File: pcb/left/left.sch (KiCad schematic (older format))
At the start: 96 parts

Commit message: pcb: left: schema
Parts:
- added D?: LED_Small, symbol Device:LED_Small
- added R?: 10K, symbol Device:R_Small
- added R?: 470, symbol Device:R_Small
- added U?: MCP23018_SO, Package_SO:SOIC-28W_7.5x17.9mm_P1.27mm, symbol symbols:MCP23018_SO
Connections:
- net labels added: COL0, COL1, COL10, COL2, COL3, COL4, COL5, COL6, COL7, COL8, COL9, ROW0, ROW1, ROW2, ROW3
- wire segments 144 -> 149
- no-connect marks 0 -> 2
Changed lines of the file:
@@
 	6650 1300 6150 1300
 Connection ~ 6650 1300
+$Comp
+L symbols:MCP23018_SO U?
+U 1 1 603DE333
+P 2350 4150
+F 0 "U?" H 2300 3800 50  0000 C CNN
+F 1 "MCP23018_SO" H 2200 3650 50  0000 C CNN
+F 2 "Package_SO:SOIC-28W_7.5x17.9mm_P1.27mm" H 2550 3150 50  0001 L CNN
+F 3 "http://ww1.microchip.com/downloads/en/DeviceDoc/20001952C.pdf" H 2550 3050 50  0001 L CNN
+	1    2350 4150
+	1    0    0    -1
+$EndComp
+$Comp
+L power:GND #PWR?
+U 1 1 603E8C90
+P 2350 5250
+F 0 "#PWR?" H 2350 5000 50  0001 C CNN
+F 1 "GND" H 2355 5077 50  0000 C CNN
+F 2 "" H 2350 5250 50  0001 C CNN
+F 3 "" H 2350 5250 50  0001 C CNN
+	1    2350 5250
+	1    0    0    -1
+$EndComp
+$Comp
+L power:GND #PWR?
+U 1 1 603F7DD2
+P 1650 4950
+F 0 "#PWR?" H 1650 4700 50  0001 C CNN
+F 1 "GND" H 1655 4777 50  0000 C CNN
+F 2 "" H 1650 4950 50  0001 C CNN
+F 3 "" H 1650 4950 50  0001 C CNN
+	1    1650 4950
+	1    0    0    -1
+$EndComp
+NoConn ~ 1650 3850
+NoConn ~ 1650 3950
+$Comp
+L power:+5V #PWR?
+U 1 1 6040C295
+P 1150 4300
+F 0 "#PWR?" H 1150 4150 50  0001 C CNN
+F 1 "+5V" H 1165 4473 50  0000 C CNN
+F 2 "" H 1150 4300 50  0001 C CNN
+F 3 "" H 1150 4300 50  0001 C CNN
+	1    1150 4300
+	1    0    0    -1
+$EndComp
+$Comp
+L Device:R_Small R?
+U 1 1 6040E182
+P 1400 4300
+F 0 "R?" V 1204 4300 50  0000 C CNN
+F 1 "10K" V 1295 4300 50  0000 C CNN
+F 2 "" H 1400 4300 50  0001 C CNN
+F 3 "~" H 1400 4300 50  0001 C CNN
+	1    1400 4300
+	0    1    1    0
+$EndComp
+Wire Wire Line
+	1150 4300 1300 4300
+Wire Wire Line
+	1500 4300 1650 4300
+$Comp
+L power:+5V #PWR?
+U 1 1 60422DB8
+P 2350 3050
+F 0 "#PWR?" H 2350 2900 50  0001 C CNN
+F 1 "+5V" H 2365 3223 50  0000 C CNN
+F 2 "" H 2350 3050 50  0001 C CNN
+F 3 "" H 2350 3050 50  0001 C CNN
+	1    2350 3050
+	1    0    0    -1
+$EndComp
+Text Label 1450 3350 0    50   ~ 0
+SCL
+Text Label 1450 3450 0    50   ~ 0
+SDA
+Wire Wire Line
+	1450 3350 1650 3350
+Wire Wire Line
+	1450 3450 1650 3450
+Text Label 6150 1300 0    50   ~ 0
+COL0
+Text Label 6150 1950 0    50   ~ 0
+COL1
+Text Label 6150 2600 0    50   ~ 0
+COL2
+Text Label 6150 3250 0    50   ~ 0
+COL3
+Text Label 6150 3900 0    50   ~ 0
+COL4
+Text Label 10600 4550 2    50   ~ 0
+COL5
+Text Label 10600 3900 2    50   ~ 0
+COL6
+Text Label 10600 3250 2    50   ~ 0
+COL7
+Text Label 10600 2600 2    50   ~ 0
+COL8
+Text Label 10600 1950 2    50   ~ 0
+COL9
+Text Label 10600 1300 2    50   ~ 0
+COL10
+Text Label 6850 4800 1    50   ~ 0
+ROW0
+Text Label 7250 4800 1    50   ~ 0
+ROW1
+Text Label 7650 4800 1    50   ~ 0
+ROW2
+Text Label 8050 4800 1    50   ~ 0
+ROW3
+Text Label 3050 4250 0    50   ~ 0
+COL0
+Text Label 3050 4350 0    50   ~ 0
+COL1
+Text Label 3050 4450 0    50   ~ 0
+COL2
+Text Label 3050 4550 0    50   ~ 0
+COL3
+Text Label 3050 4650 0    50   ~ 0
+COL4
+Text Label 3050 4750 0    50   ~ 0
+COL5
+Text Label 3050 4850 0    50   ~ 0
+COL6
+Text Label 3050 4950 0    50   ~ 0
+COL7
+Text Label 3050 3350 0    50   ~ 0
+COL8
+Text Label 3050 3450 0    50   ~ 0
+COL9
+Text Label 3050 3550 0    50   ~ 0
+COL10
+Text Label 3050 3650 0    50   ~ 0
+ROW0
+Text Label 3050 3750 0    50   ~ 0
+ROW1
+Text Label 3050 3850 0    50   ~ 0
+ROW2
+Text Label 3050 3950 0    50   ~ 0
+ROW3
+Wire Wire Line
+	3050 4050 3600 4050
+$Comp
+L Device:LED_Small D?
+U 1 1 604A9BDF
+P 3600 3950
+F 0 "D?" V 3646 3880 50  0000 R CNN
+F 1 "LED_Small" V 3555 3880 50  0000 R CNN
+F 2 "" V 3600 3950 50  0001 C CNN
+F 3 "~" V 3600 3950 50  0001 C CNN
+	1    3600 3950
+	0    -1   -1   0
+$EndComp
+$Comp
+L Device:R_Small R?
+U 1 1 604AA823
+P 3600 3750
+F 0 "R?" H 3659 3796 50  0000 L CNN
+F 1 "470" H 3659 3705 50  0000 L CNN
+F 2 "" H 3600 3750 50  0001 C CNN
+F 3 "~" H 3600 3750 50  0001 C CNN
+	1    3600 3750
+	1    0    0    -1
+$EndComp
+$Comp
+L power:+5V #PWR?
+U 1 1 604AB14C
+P 3600 3650
+F 0 "#PWR?" H 3600 3500 50  0001 C CNN
+F 1 "+5V" H 3615 3823 50  0000 C CNN
+F 2 "" H 3600 3650 50  0001 C CNN
+F 3 "" H 3600 3650 50  0001 C CNN
+	1    3600 3650
+	1    0    0    -1
+$EndComp
 $EndSCHEMATC

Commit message: pcb: left: annotate
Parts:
- gave numbers to parts that had none: 100
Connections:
- no-connect marks 2 -> 3

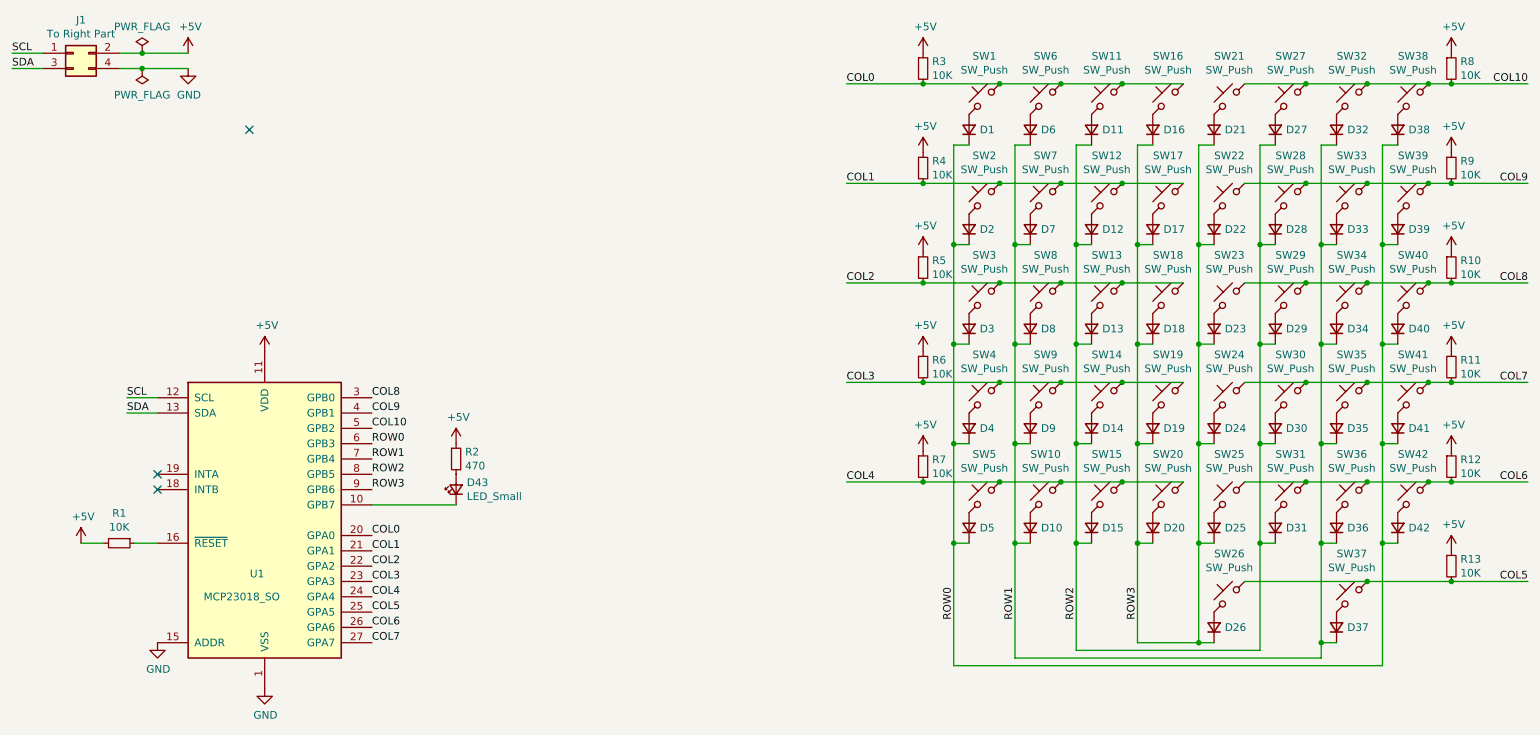
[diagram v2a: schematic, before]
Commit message: pcb: left: assign footprints
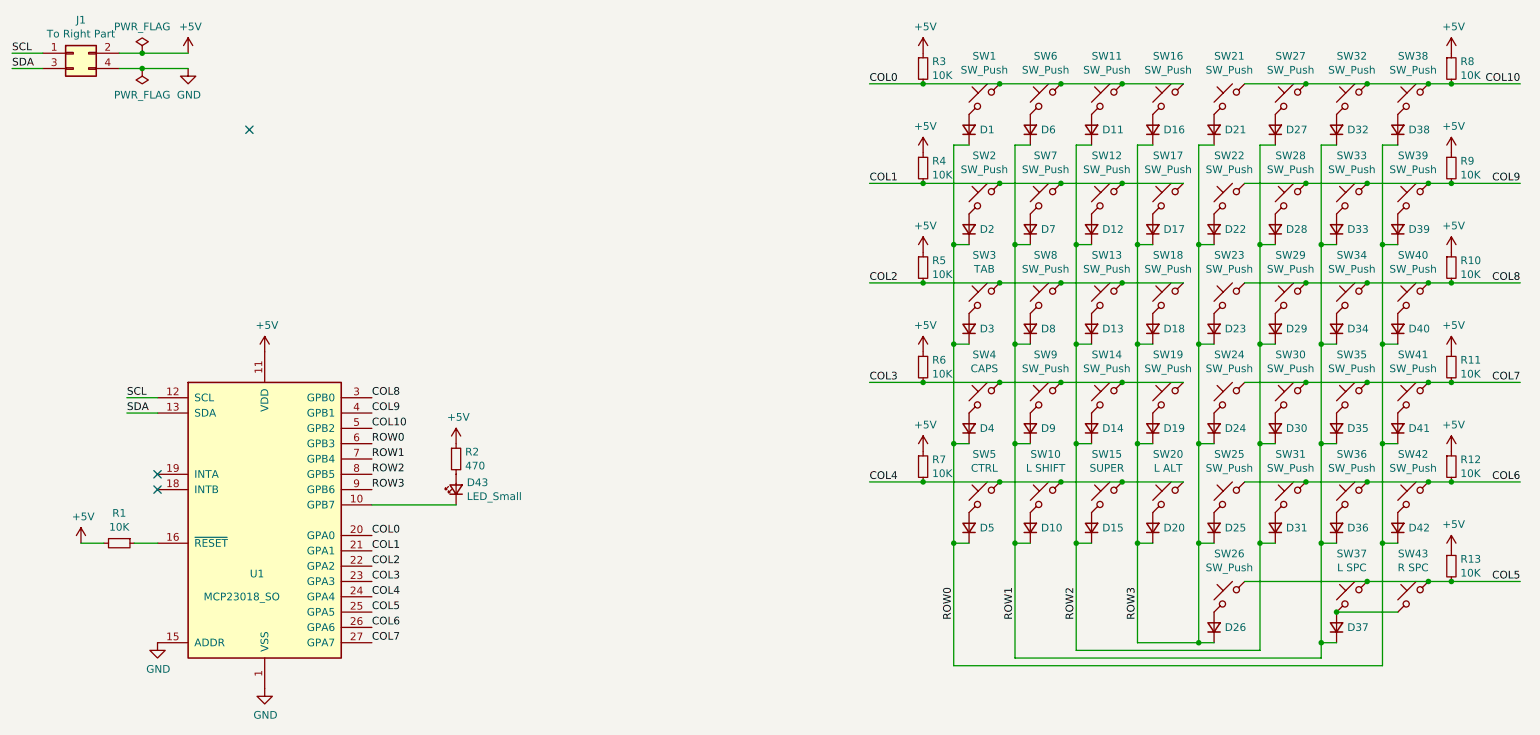
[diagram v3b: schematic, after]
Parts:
- added SW43: R SPC, Button_Switch_Keyboard:SW_Cherry_MX_2.25u_PCB, symbol Switch:SW_Push_45deg
- D1, D10, D11, D12, D13, D14, D15, D16, D17, D18, D19, D2, D20, D21, D22, D23, D24, D25, D26, D27, D28, D29, D3, D30, D31, D32, D33, D34, D35, D36, D37, D38, D39, D4, D40, D41, D42, D5, D6, D7, D8, D9: footprint (none) -> Diode_SMD:D_SOD-123
- D43: footprint (none) -> LED_SMD:LED_0805_2012Metric_Pad1.15x1.40mm_HandSolder
- J1: footprint (none) -> Connector_PinHeader_2.54mm:PinHeader_2x02_P2.54mm_Vertical
- R1, R10, R11, R12, R13, R2, R3, R4, R5, R6, R7, R8, R9: footprint (none) -> Resistor_SMD:R_0805_2012Metric_Pad1.20x1.40mm_HandSolder
- SW1, SW11, SW12, SW13, SW14, SW16, SW17, SW18, SW19, SW2, SW21, SW22, SW23, SW24, SW25, SW26, SW27, SW28, SW29, SW30, SW31, SW32, SW33, SW34, SW35, SW36, SW38, SW39, SW40, SW41, SW42, SW6, SW7, SW8, SW9: footprint (none) -> Button_Switch_Keyboard:SW_Cherry_MX_1.00u_PCB
- SW10: value SW_Push -> L SHIFT; footprint (none) -> Button_Switch_Keyboard:SW_Cherry_MX_2.25u_PCB
- SW15: value SW_Push -> SUPER; footprint (none) -> Button_Switch_Keyboard:SW_Cherry_MX_1.25u_PCB
- SW20: value SW_Push -> L ALT; footprint (none) -> Button_Switch_Keyboard:SW_Cherry_MX_1.25u_PCB
- SW3: value SW_Push -> TAB; footprint (none) -> Button_Switch_Keyboard:SW_Cherry_MX_1.50u_PCB
- SW37: value SW_Push -> L SPC; footprint (none) -> Button_Switch_Keyboard:SW_Cherry_MX_2.75u_PCB
- SW4: value SW_Push -> CAPS; footprint (none) -> Button_Switch_Keyboard:SW_Cherry_MX_1.75u_PCB
- SW5: value SW_Push -> CTRL; footprint (none) -> Button_Switch_Keyboard:SW_Cherry_MX_1.25u_PCB
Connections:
- net COL5: now also SW43.1
- net at D37.2 (A), SW37.2: now also SW43.2
